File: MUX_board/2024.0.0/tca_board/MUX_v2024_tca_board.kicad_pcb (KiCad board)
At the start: 2 copper layers, 80 x 55 mm, 14 parts, among them J1 I2C, J2 I2C, J3 I2C, J4 I2C, J5 I2C, J6 I2C, J7 I2C, J8 I2C, J9 I2C

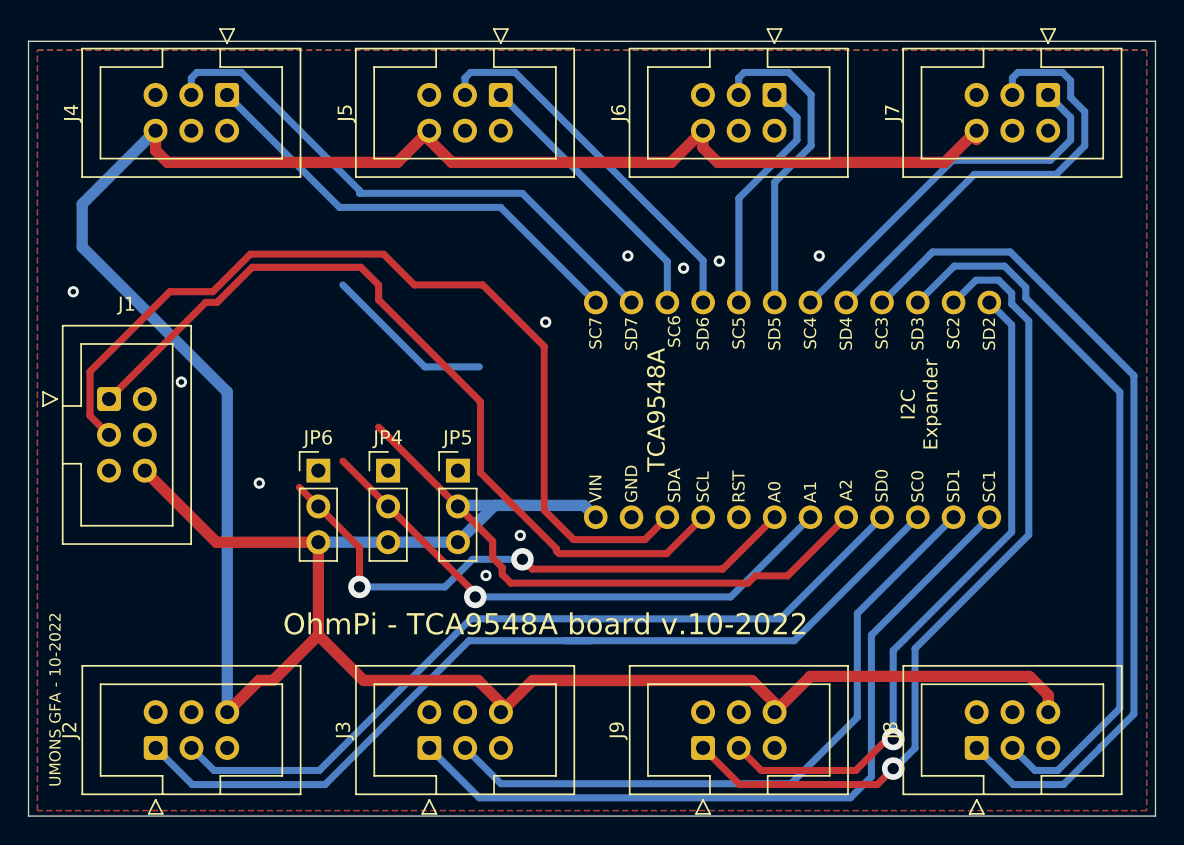
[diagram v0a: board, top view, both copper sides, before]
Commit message: Improves TCA board PCB design
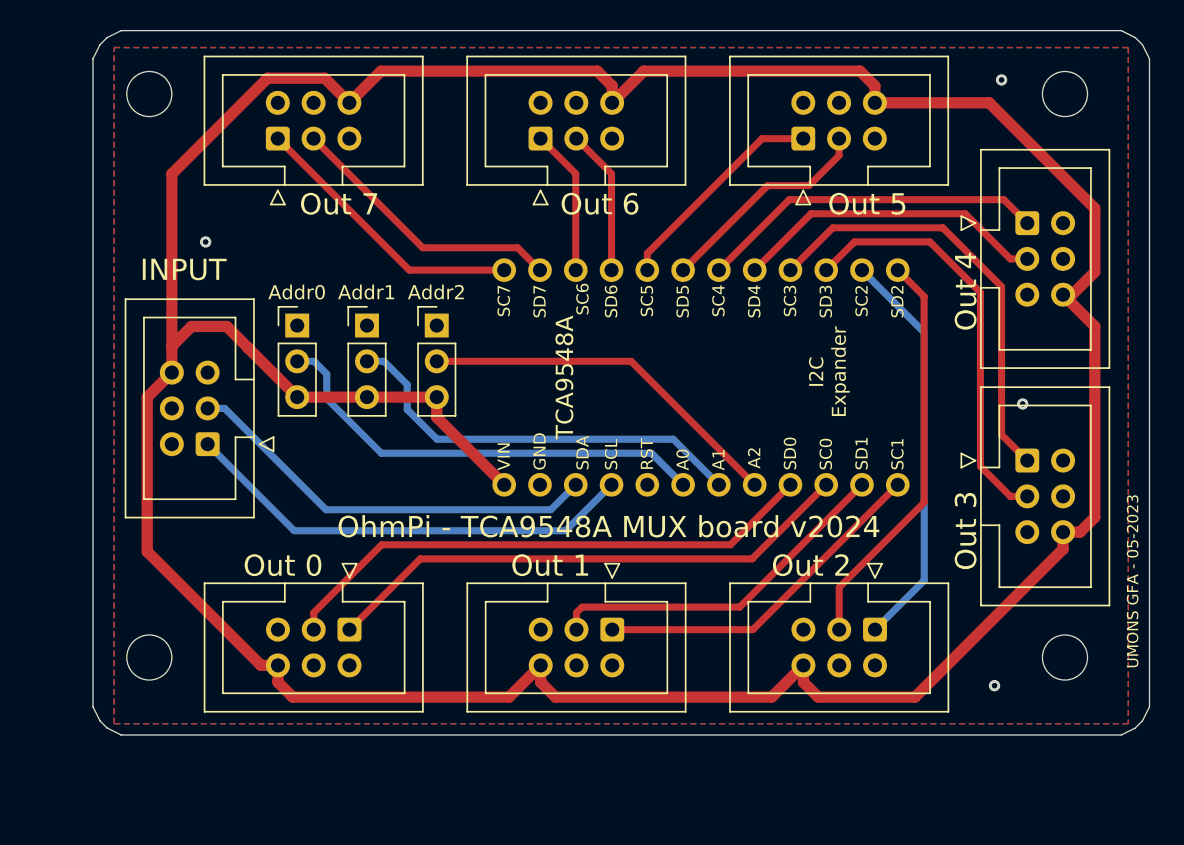
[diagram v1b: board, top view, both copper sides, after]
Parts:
- added REF**: MountingHole_3.2mm_M3_ISO7380, MountingHole:MountingHole_3.2mm_M3_ISO7380, F.Cu at (107.0, 115.5)
- added REF**: MountingHole_3.2mm_M3_ISO7380, MountingHole:MountingHole_3.2mm_M3_ISO7380, F.Cu at (172.0, 115.5)
- added REF**: MountingHole_3.2mm_M3_ISO7380, MountingHole:MountingHole_3.2mm_M3_ISO7380, F.Cu at (107.0, 75.5)
- added REF**: MountingHole_3.2mm_M3_ISO7380, MountingHole:MountingHole_3.2mm_M3_ISO7380, F.Cu at (172.0, 75.5)
- Addr0: renamed from JP6; value Addr 0 -> Addr0
- moved J8 20.7 mm to (169.3, 101.5), turned to 0 degrees
- moved J2 16.1 mm to (121.2, 113.5), turned to -90 degrees
- moved J3 15.5 mm to (139.9, 113.5), turned to -90 degrees
- moved J9 14.8 mm to (158.5, 113.5), turned to -90 degrees
- moved Addr0 10.4 mm to (117.5, 91.9)
- moved Addr1 10.4 mm to (122.5, 91.9)
- moved Addr2 10.4 mm to (127.4, 91.9)
- moved J7 9.22 mm to (169.3, 84.7), turned to 0 degrees
- moved J1 7.70 mm to (111.1, 100.4), turned to 180 degrees
- moved JP1 6.89 mm to (146.2, 88.0)
- moved JP3 6.89 mm to (146.2, 103.2)
- moved J4 4.75 mm to (116.1, 78.7), turned to 90 degrees
- moved J5 4.19 mm to (134.8, 78.7), turned to 90 degrees
- moved J6 3.71 mm to (153.4, 78.7), turned to 90 degrees
- renumbered JP4 to Addr1, JP5 to Addr2
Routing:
- net /INPUTSDA: track 65.3 -> 29.8 mm
- net /1SCL: track 55.4 -> 24.5 mm
- net /3SCL: track 61.3 -> 31.1 mm
- net /2SCL: track 58.5 -> 28.8 mm, vias 1 -> 0
- net +5V: track 269.5 -> 242.1 mm
- net /0SCL: track 64.9 -> 38.1 mm
- net /INPUTSCL: track 59.0 -> 32.6 mm
- net /A2: track 0.00 -> 26.2 mm
- net /1SDA: track 47.9 -> 25.2 mm
- net /3SDA: track 52.1 -> 29.8 mm
- net /7SDA: track 39.5 -> 19.9 mm
- net /2SDA: track 47.7 -> 28.8 mm, vias 1 -> 0
- net /0SDA: track 57.1 -> 38.8 mm
- net /6SDA: track 26.8 -> 10.4 mm
- net /7SCL: track 32.3 -> 19.9 mm
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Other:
- board size 80 x 55 mm -> 75 x 50 mm
- board text added: "INPUT"
- board text added: "OhmPi - TCA9548A MUX board v2024"
- board text added: "Out 0"
- board text added: "Out 1"
- board text added: "Out 2"
- board text added: "Out 3"
- board text added: "Out 4"
- board text added: "Out 5"
- board text added: "Out 6"
- board text added: "Out 7"
- board text added: "UMONS GFA - 05-2023"
- board text removed: "OhmPi - TCA9548A board v.10-2022"
- board text removed: "UMONS GFA - 10-2022"
